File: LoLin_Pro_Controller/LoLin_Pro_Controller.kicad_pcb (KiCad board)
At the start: 2 copper layers, 85.1 x 86.1 mm, 30 parts, among them J1 Conn_01x03, J10 Volt_Sel, J2 Conn_01x03, J3 Conn_01x03, J4 Conn_01x03, J5 Conn_01x03, J6 Conn_01x03, M1 LolinD32, U2 LM7805_TO220, U3 SN74HCT245N

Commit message: added gerbers
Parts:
- moved F3 6.60 mm to (147.8, 124.5)
- moved F5 6.60 mm to (160.3, 124.5)
- moved C1 6.60 mm to (126.6, 93.8)
- moved C2 6.60 mm to (138.7, 80.2)
- moved C3 6.60 mm to (179.8, 85.6)
- moved F1 6.60 mm to (136.1, 124.5)
- moved F2 6.60 mm to (142.0, 124.5)
- moved F4 6.60 mm to (153.9, 124.5)
- moved F6 6.60 mm to (166.6, 124.5)
- moved F9 6.60 mm to (126.5, 115.1)
- moved J1 6.60 mm to (136.6, 97.5)
- moved J10 6.60 mm to (128.3, 86.0)
- moved J2 6.60 mm to (136.6, 110.0)
- moved J3 6.60 mm to (151.4, 97.5)
- moved J4 6.60 mm to (151.4, 110.0)
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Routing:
- net Net-(M1-Pad5): track 18.9 -> 13.7 mm
- net Net-(M1-Pad10): track 8.49 -> 12.9 mm
- net Net-(M1-Pad11): track 8.49 -> 12.1 mm
- net Net-(M1-Pad6): track 11.6 -> 8.14 mm, vias 1 -> 0
- net Net-(M1-Pad4): track 21.7 -> 19.3 mm, vias 0 -> 1
- net Net-(M1-Pad19): track 62.4 -> 64.6 mm
- net Net-(J3-Pad2): track 9.93 -> 8.67 mm
- net /VOUT5: track 31.1 -> 32.2 mm
- net /VOUT3: track 32.5 -> 31.5 mm
- net +5V: track 83.1 -> 83.8 mm
- net /VOUT6: track 15.0 -> 15.5 mm
- net GND: vias 0 -> 44
- net +VDC: vias 0 -> 5
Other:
- board text removed: "Short for 5v In"

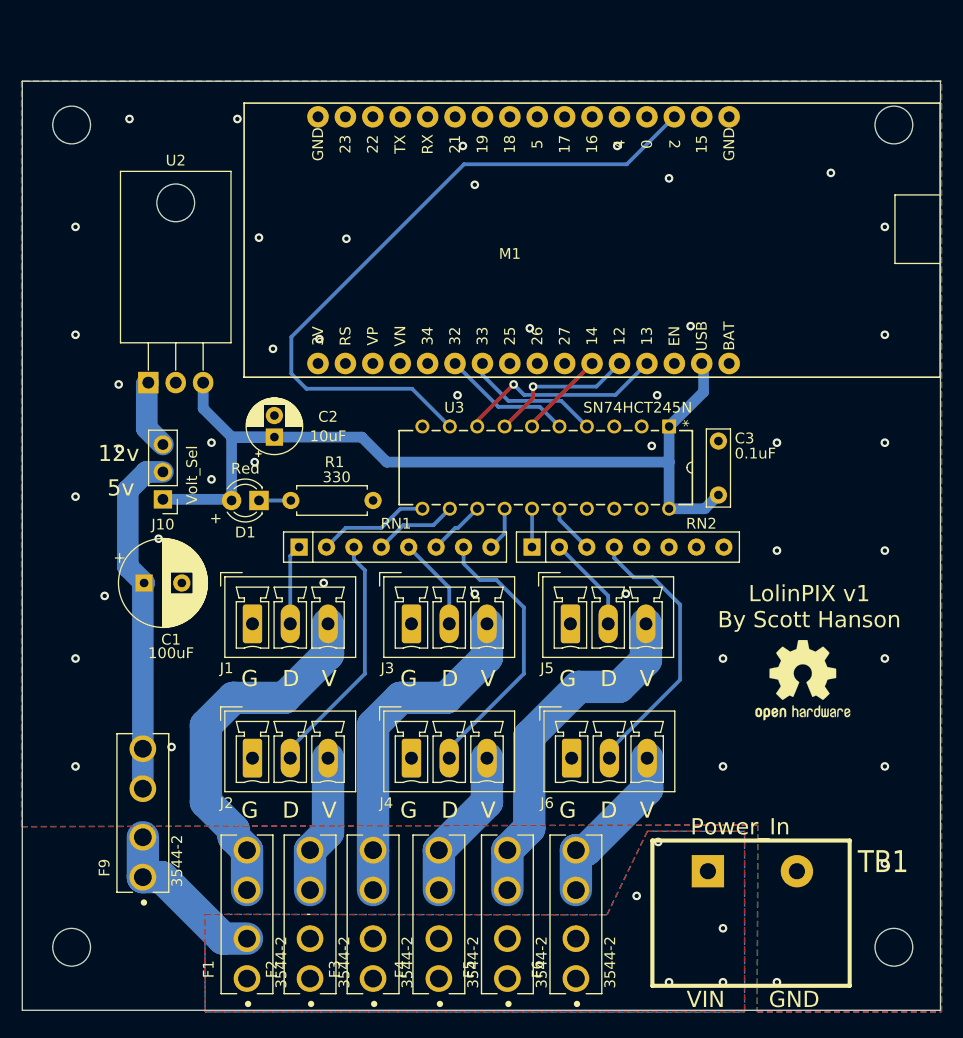
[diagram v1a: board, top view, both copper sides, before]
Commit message: added OLED
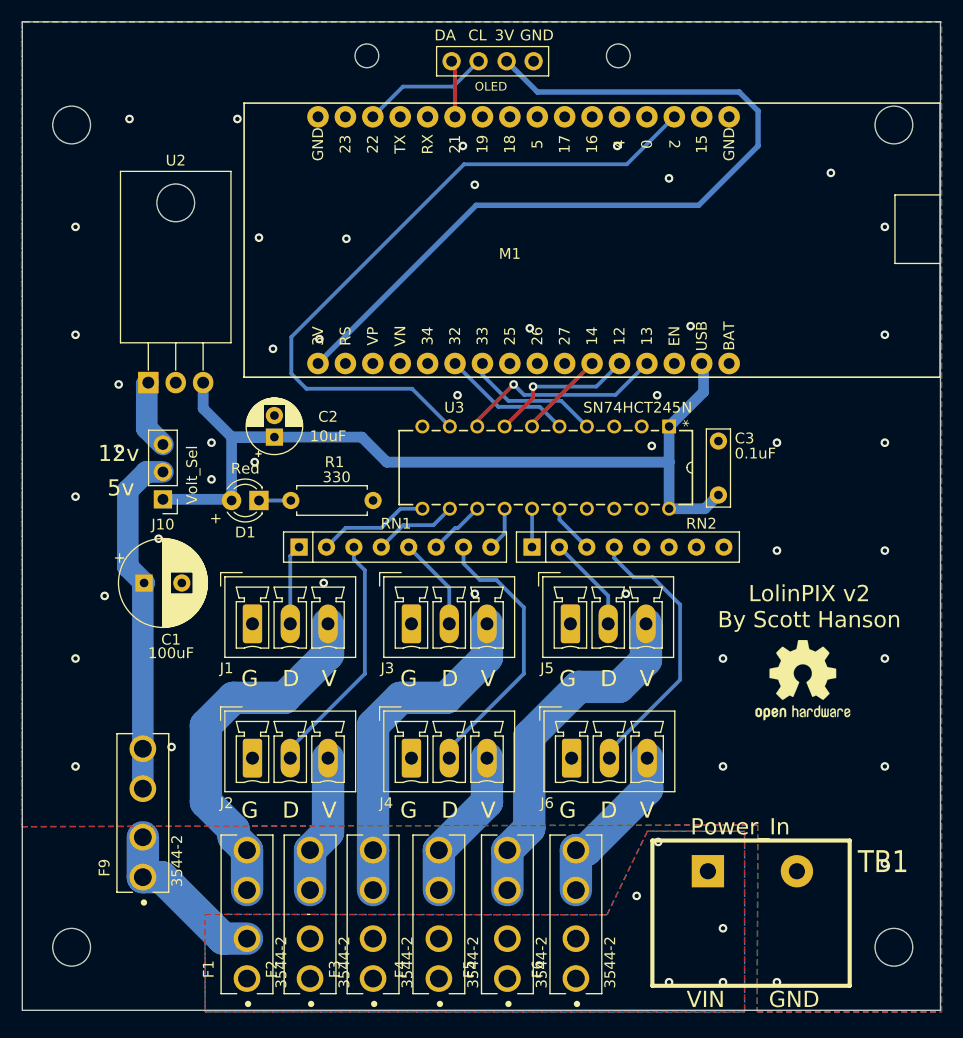
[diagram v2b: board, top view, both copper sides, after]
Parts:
- added J7: OLED, OLED-SSD1306-128X64-I2C:OLED-SSD1306-128X64-I2C-THT, F.Cu at (158.9, 45.4)
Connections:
- M1 pad 16: Net-(M1-Pad16) -> +3V3
- M1 pad 27: Net-(M1-Pad27) -> I2C_SDA
- M1 pad 30: Net-(M1-Pad30) -> I2C_SCL
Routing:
- net +3V3: track 0.00 -> 77.6 mm
- net I2C_SCL: track 0.00 -> 11.9 mm
- net I2C_SDA: track 0.00 -> 5.28 mm
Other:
- board size 85.1 x 86.1 mm -> 85.1 x 91.6 mm
- net class 3v added: clearance 0.2, trace_width 0.5, via_dia 0.8, via_drill 0.4
- board text added: "3V"
- board text added: "CL"
- board text added: "DA"
- board text added: "LolinPIX v2 By Scott Hanson"
- board text removed: "LolinPIX v1 By Scott Hanson"
